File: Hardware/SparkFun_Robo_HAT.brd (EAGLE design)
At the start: 64.9 x 56.1 mm, 227 parts, among them J1 RASPBERRYPI-40-PIN-GPIO_PTH_R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, J11 EXT MTR PWR, J18 ISP, J2 CORTEX_DEBUGPTH, J20 USB C, J7 EXT SERVO PWR, J8 EXT 5V PWR, Q1 310mA/60V/1.6Ω, Q23 20V/0.2A/8MHz/1.2Ω/1Vth, Q24 20V/0.2A/8MHz/1.2Ω/1Vth, Q27 20V/0.2A/8MHz/1.2Ω/1Vth, Q28 20V/0.2A/8MHz/1.2Ω/1Vth, Q4 310mA/60V/1.6Ω, Q5 20V/4.2A/52mΩ/1.4W, Q7 20V/4.2A/52mΩ/1.4W, Q9 20V/4.2A/52mΩ/1.4W, U1 PCA9685, U4 ATTINY84-ARDUINO, U5 DRV8835, U6 CY8C4245LQI-483, U7 9DoF IMU, U8 1.8V/100mA

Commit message: sch cleanup and drc stuff in brd
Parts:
- removed J2: CORTEX_DEBUGPTH, Pete_Connectors_Retired:2X5-PTH-1.27MM
- removed TP19: (no value), SparkFun-Connectors:TP_15TH
- added J23: CORTEX_JTAG_DEBUG_PTH, SparkFun-Connectors:2X5-PTH-1.27MM
- added TP9: (no value), SparkFun-Connectors:PAD.03X.03
- TP5: value 1.8V -> (none); device SparkFun-Connectors:PAD.03X.03 -> SparkFun-Connectors:TP_15TH
- moved TP5 41.2 mm to (61.0, 8.89), flipped to the top, turned to 270 degrees
- moved FRAME1 32.1 mm to (26.7, -20.3)
- moved R10 0.18 mm to (8.88, 42.3)
- moved C10 0.07 mm to (8.13, 39.9)
- renumbered TP11 to TP7, TP12 to TP8, TP18 to TP4, TP24 to TP6
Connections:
- net !MTR_RST: now also J23.10; no longer J2.10
- net 1.8V: now also TP9.P$1; no longer TP5.P$1
- net 3.3V: now also J23.1; no longer J2.1
- net GND: now also J23.3, J23.5, J23.7, J23.9; no longer J2.3, J2.5, J2.7, J2.9
- net P3.2: now also J23.2; no longer J2.2
- net P3.3: now also J23.4; no longer J2.4
- net SDA_3.3V: now also TP5.P$1; no longer TP19.P$1
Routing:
- net PI-5V: track 13.8 -> 13.1 mm
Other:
- board size 64.9 x 56.1 mm -> 64.9 x 55.9 mm
- board text added: "Servo Controller based on a design by Mike Hord Serial Controlled Motor Driver based on designs by Marshall Taylor, Alex Wende ICM-20948 based on a design by Owen Lyke ATTINY84 Encoder based on a design by Nathan Seidle"
- board text removed: "ATTiny84 Encoder based on a design by Nathan Seidle"
- board text removed: "ICM-20948 IMU based on a design by Owen Lyke"
- board text removed: "Serial Controlled Motor Driver based on a design by Marshall Taylor, Alex Wende"
- board text removed: "Servo Controller based on a design by Mike Hord"

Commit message: removed USB C Shield polygon
to let more GND flow under connector up to Pi Header.
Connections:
- removed net SHLD: J20.SHLD1, J20.SHLD2, J20.SHLD3, J20.SHLD4, J20.SHLD5, J20.SHLD6, J20.SHLD7, J20.SHLD8
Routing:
- net SHLD: track 0.59 -> 0.00 mm
- removed copper zone on layer 1, net SHLD
- removed copper zone on layer 16, net SHLD
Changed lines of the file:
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@@
 <layer number="37" name="tTest" color="7" fill="1" visible="no" active="yes"/>
 <layer number="38" name="bTest" color="7" fill="1" visible="no" active="yes"/>
-<layer number="39" name="tKeepout" color="4" fill="11" visible="yes" active="yes"/>
+<layer number="39" name="tKeepout" color="4" fill="11" visible="no" active="yes"/>
 <layer number="40" name="bKeepout" color="1" fill="11" visible="no" active="yes"/>
 <layer number="41" name="tRestrict" color="4" fill="10" visible="no" active="yes"/>
@@
 <wire x1="18.201640625" y1="44.223940625" x2="18.191478125" y2="44.213778125" width="0.508" layer="16"/>
 </signal>
-<signal name="SHLD">
-<contactref element="J20" pad="SHLD2"/>
-<contactref element="J20" pad="SHLD4"/>
-<contactref element="J20" pad="SHLD1"/>
-<contactref element="J20" pad="SHLD6"/>
-<contactref element="J20" pad="SHLD3"/>
-<contactref element="J20" pad="SHLD7"/>
-<contactref element="J20" pad="SHLD5"/>
-<contactref element="J20" pad="SHLD8"/>
-<polygon width="0.254" layer="1" orphans="yes">
-<vertex x="0.254" y="48.895"/>
-<vertex x="2.64921875" y="48.895"/>
-<vertex x="2.64921875" y="38.354"/>
-<vertex x="0.254" y="38.354"/>
-</polygon>
-<polygon width="0.254" layer="16" orphans="yes">
-<vertex x="0.254" y="48.895"/>
-<vertex x="2.649221875" y="48.895"/>
-<vertex x="2.649221875" y="38.354"/>
-<vertex x="0.254" y="38.354"/>
-</polygon>
-<wire x1="5.435" y1="47.881" x2="5.1694" y2="47.881" width="0.2032" layer="1"/>
-<wire x1="5.435" y1="39.241" x2="5.1694" y2="39.241" width="0.2032" layer="1"/>
-<wire x1="1.255" y1="39.241" x2="1.2856" y2="39.241" width="0.2032" layer="1"/>
-<wire x1="1.255" y1="47.881" x2="1.2856" y2="47.881" width="0.2032" layer="1"/>
-<wire x1="5.435" y1="47.881" x2="5.435" y2="47.881" width="0" layer="19" extent="1-16"/>
-<wire x1="1.2856" y1="47.881" x2="5.1694" y2="47.881" width="0" layer="19" extent="1-1"/>
-<wire x1="1.255" y1="47.881" x2="1.255" y2="47.881" width="0" layer="19" extent="1-16"/>
-<wire x1="5.435" y1="39.241" x2="5.435" y2="47.881" width="0" layer="19" extent="16-16"/>
-<wire x1="5.435" y1="39.241" x2="5.435" y2="39.241" width="0" layer="19" extent="1-16"/>
-<wire x1="1.2856" y1="39.241" x2="5.1694" y2="39.241" width="0" layer="19" extent="1-1"/>
-<wire x1="1.255" y1="39.241" x2="1.255" y2="39.241" width="0" layer="19" extent="1-16"/>
-</signal>
 <signal name="CC2">

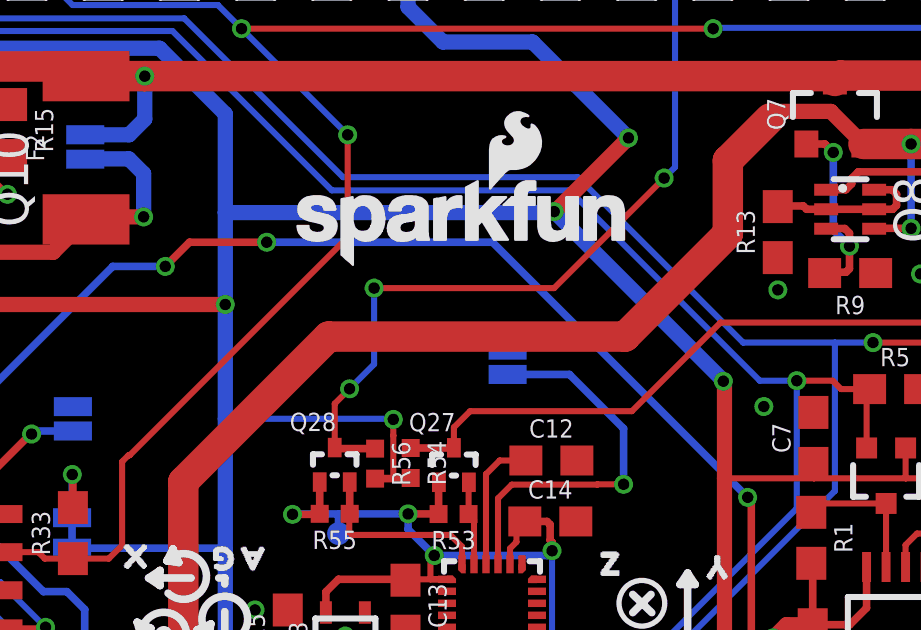
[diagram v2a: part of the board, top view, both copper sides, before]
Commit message: added product name to top silk
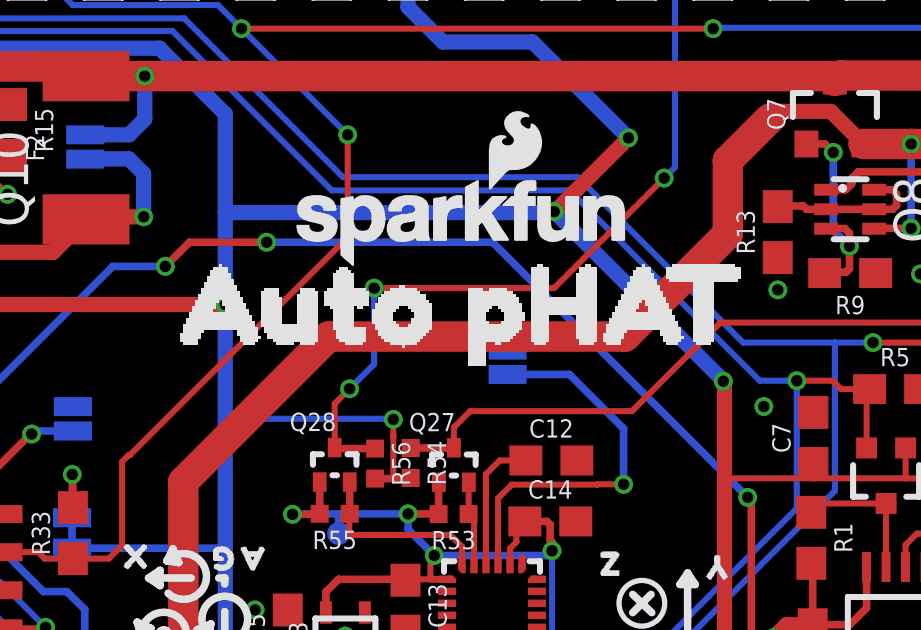
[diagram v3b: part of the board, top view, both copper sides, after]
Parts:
- added U$83: (no value), buzzard_labels (9):AUTO_PHAT0
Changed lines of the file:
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@@
 <attribute name="VALUE" x="39.9288" y="21.5138" size="0.6096" layer="27" font="vector" ratio="20" rot="R180"/>
 </element>
+<element name="U$83" library="buzzard_labels (9)" package="AUTO_PHAT0" value="" x="19.05" y="39.37" smashed="yes"/>
 </elements>
 <signals>

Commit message: flipped I2C label to match others, added name to bsilk, aligned other labels
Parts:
- added U$84: (no value), buzzard_labels (9):AUTO_PHAT0
- moved LOGO1 19.9 mm to (32.0, 45.8)
- moved U$2 2.96 mm to (49.7, 39.6), turned to 0 degrees
- moved U$54 0.48 mm to (63.3, 43.1)
- moved U$53 0.43 mm to (63.2, 48.2)
- moved U$59 0.36 mm to (63.2, 45.7)
- moved U$60 0.35 mm to (63.2, 40.6)
- moved U$55 0.25 mm to (63.2, 38.0)
- moved U$61 0.24 mm to (63.1, 35.5)
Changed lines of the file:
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@@
 <grid distance="0.05" unitdist="inch" unit="inch" style="lines" multiple="1" display="yes" altdistance="0.0001" altunitdist="inch" altunit="inch"/>
 <layers>
-<layer number="1" name="Top" color="4" fill="1" visible="yes" active="yes"/>
+<layer number="1" name="Top" color="4" fill="1" visible="no" active="yes"/>
 <layer number="15" name="Route15" color="4" fill="6" visible="no" active="no"/>
 <layer number="16" name="Bottom" color="1" fill="1" visible="yes" active="yes"/>
 <layer number="17" name="Pads" color="2" fill="1" visible="yes" active="yes"/>
 <layer number="18" name="Vias" color="2" fill="1" visible="yes" active="yes"/>
-<layer number="19" name="Unrouted" color="6" fill="1" visible="yes" active="yes"/>
-<layer number="20" name="Dimension" color="24" fill="1" visible="yes" active="yes"/>
-<layer number="21" name="tPlace" color="16" fill="1" visible="yes" active="yes"/>
+<layer number="19" name="Unrouted" color="6" fill="1" visible="no" active="yes"/>
+<layer number="20" name="Dimension" color="24" fill="1" visible="no" active="yes"/>
+<layer number="21" name="tPlace" color="16" fill="1" visible="no" active="yes"/>
 <layer number="22" name="bPlace" color="14" fill="1" visible="yes" active="yes"/>
-<layer number="23" name="tOrigins" color="15" fill="1" visible="yes" active="yes"/>
+<layer number="23" name="tOrigins" color="15" fill="1" visible="no" active="yes"/>
 <layer number="24" name="bOrigins" color="15" fill="1" visible="yes" active="yes"/>
 <layer number="25" name="tNames" color="7" fill="1" visible="no" active="yes"/>
@@
 <layer number="28" name="bValues" color="7" fill="1" visible="no" active="yes"/>
 <layer number="29" name="tStop" color="7" fill="3" visible="no" active="yes"/>
-<layer number="30" name="bStop" color="7" fill="6" visible="no" active="yes"/>
+<layer number="30" name="bStop" color="7" fill="6" visible="yes" active="yes"/>
 <layer number="31" name="tCream" color="7" fill="4" visible="no" active="yes"/>
 <layer number="32" name="bCream" color="7" fill="5" visible="no" active="yes"/>
@@
 <layer number="43" name="vRestrict" color="2" fill="10" visible="no" active="yes"/>
 <layer number="44" name="Drills" color="7" fill="1" visible="no" active="yes"/>
-<layer number="45" name="Holes" color="7" fill="1" visible="yes" active="yes"/>
+<layer number="45" name="Holes" color="7" fill="1" visible="no" active="yes"/>
 <layer number="46" name="Milling" color="3" fill="1" visible="no" active="yes"/>
 <layer number="47" name="Measures" color="7" fill="1" visible="no" active="yes"/>
 <layer number="48" name="Document" color="13" fill="7" visible="no" active="yes"/>
-<layer number="49" name="Reference" color="13" fill="1" visible="yes" active="yes"/>
+<layer number="49" name="Reference" color="13" fill="1" visible="no" active="yes"/>
 <layer number="50" name="dxf" color="7" fill="1" visible="no" active="yes"/>
-<layer number="51" name="tDocu" color="6" fill="1" visible="yes" active="yes"/>
+<layer number="51" name="tDocu" color="6" fill="1" visible="no" active="yes"/>
 <layer number="52" name="bDocu" color="7" fill="1" visible="no" active="yes"/>
 <layer number="91" name="Nets" color="2" fill="1" visible="no" active="no"/>
@@
 <element name="FD1" library="SparkFun-Aesthetics" package="FIDUCIAL-MICRO" value="FIDUCIALUFIDUCIAL" x="0.828040625" y="5.4076625" smashed="yes"/>
 <element name="FD2" library="SparkFun-Aesthetics" package="FIDUCIAL-MICRO" value="FIDUCIALUFIDUCIAL" x="59.776359375" y="55.138321875" smashed="yes"/>
-<element name="LOGO1" library="SparkFun-Aesthetics" package="SFE_LOGO_NAME_FLAME_.1" value="SFE_LOGO_NAME_FLAME.1_INCH" x="45.04435625" y="30.8203625" smashed="yes" rot="MR0"/>
+<element name="LOGO1" library="SparkFun-Aesthetics" package="SFE_LOGO_NAME_FLAME_.1" value="SFE_LOGO_NAME_FLAME.1_INCH" x="32.02939375" y="45.813984375" smashed="yes" rot="MR0"/>
 <element name="LOGO2" library="SparkFun-Aesthetics" package="OSHW-LOGO-S" value="OSHW-LOGOS" x="4.5085" y="11.5824" smashed="yes"/>
 <element name="FD3" library="SparkFun-Aesthetics" package="FIDUCIAL-MICRO" value="FIDUCIALUFIDUCIAL" x="0.828040625" y="5.4076625" smashed="yes" rot="MR0"/>
@@
 <attribute name="VALUE" x="48.259996875" y="39.093140625" size="0.6096" layer="28" font="vector" ratio="20" rot="MR180" align="top-center"/>
 </element>
-<element name="U$2" library="Qwiic RFID - IDXXLA" package="I_SUPER2_C-()-03" value="" x="46.720759375" y="39.65701875" smashed="yes" rot="MR180"/>
+<element name="U$2" library="Qwiic RFID - IDXXLA" package="I_SUPER2_C-()-03" value="" x="49.684940625" y="39.588440625" smashed="yes" rot="MR0"/>
 <element name="U$32" library="buzzard_labels (3)" package="ISO1" value="" x="6.931659375" y="47.244" smashed="yes"/>
 <element name="JP4" library="SparkFun-Jumpers" package="SMT-JUMPER_2_NC_TRACE_SILK" value="PI ISO" x="10.581640625" y="47.769778125" smashed="yes" rot="R90">
@@
 <element name="U$51" library="buzzard_labels (7)" package="MTR_ADR0" value="" x="31.42488125" y="26.5684" smashed="yes" rot="MR0"/>
 <element name="U$52" library="buzzard_labels (1)" package="EXT_PWR_INPUTS3" value="" x="55.01131875" y="48.8442" smashed="yes" rot="MR270"/>
-<element name="U$53" library="buzzard_labels (6)" package="5V3" value="" x="62.78118125" y="48.270159375" smashed="yes" rot="MR0"/>
-<element name="U$54" library="buzzard_labels (6)" package="MTR4" value="" x="62.78118125" y="43.113959375" smashed="yes" rot="MR0"/>
-<element name="U$55" library="buzzard_labels (6)" package="SERVO5" value="" x="62.913259375" y="38.03141875" smashed="yes" rot="MR0"/>
+<element name="U$53" library="buzzard_labels (6)" package="5V3" value="" x="63.21298125" y="48.247296875" smashed="yes" rot="MR0"/>
+<element name="U$54" library="buzzard_labels (6)" package="MTR4" value="" x="63.2587" y="43.113959375" smashed="yes" rot="MR0"/>
+<element name="U$55" library="buzzard_labels (6)" package="SERVO5" value="" x="63.162178125" y="38.003478125" smashed="yes" rot="MR0"/>
 <element name="U$56" library="buzzard_labels (6)" package="#ENC_RST6" value="" x="63.439040625" y="30.490159375" smashed="yes" rot="MR0"/>
 <element name="U$57" library="buzzard_labels (6)" package="#MTR_RST7" value="" x="63.535559375" y="27.810459375" smashed="yes" rot="MR0"/>
 <element name="U$58" library="buzzard_labels (6)" package="#FSYNC8" value="" x="63.433959375" y="25.397459375" smashed="yes" rot="MR0"/>
-<element name="U$59" library="buzzard_labels" package="GND3" value="" x="62.875159375" y="45.697140625" smashed="yes" rot="MR0"/>
-<element name="U$60" library="buzzard_labels" package="GND3" value="" x="62.849759375" y="40.54601875" smashed="yes" rot="MR0"/>
-<element name="U$61" library="buzzard_labels" package="GND3" value="" x="62.900559375" y="35.49141875" smashed="yes" rot="MR0"/>
+<element name="U$59" library="buzzard_labels" package="GND3" value="" x="63.235840625" y="45.697140625" smashed="yes" rot="MR0"/>
+<element name="U$60" library="buzzard_labels" package="GND3" value="" x="63.197740625" y="40.5638" smashed="yes" rot="MR0"/>
+<element name="U$61" library="buzzard_labels" package="GND3" value="" x="63.13931875" y="35.514278125" smashed="yes" rot="MR0"/>
 <element name="U$62" library="buzzard_labels (8)" package="#ENC_INT0" value="" x="63.433959375" y="33.017459375" smashed="yes" rot="MR0"/>
 <element name="U$63" library="buzzard_labels (2)" package="#16" value="" x="18.79091875" y="1.397" smashed="yes" rot="MR0"/>
@@
 </element>
 <element name="U$83" library="buzzard_labels (9)" package="AUTO_PHAT0" value="" x="19.05" y="39.37" smashed="yes"/>
+<element name="U$84" library="buzzard_labels (9)" package="AUTO_PHAT0" value="" x="44.074078125" y="42.72788125" smashed="yes" rot="MR0"/>
 </elements>
 <signals>
